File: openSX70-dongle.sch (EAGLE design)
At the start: 22 parts

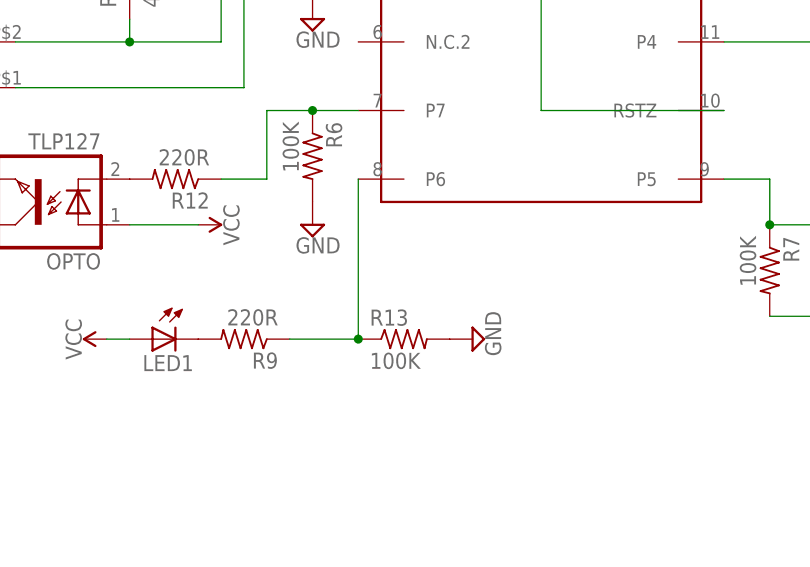
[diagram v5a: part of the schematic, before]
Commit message: P7 and P6 had a pulldown resistor when a pullup was needed. More D'ho! stuff.
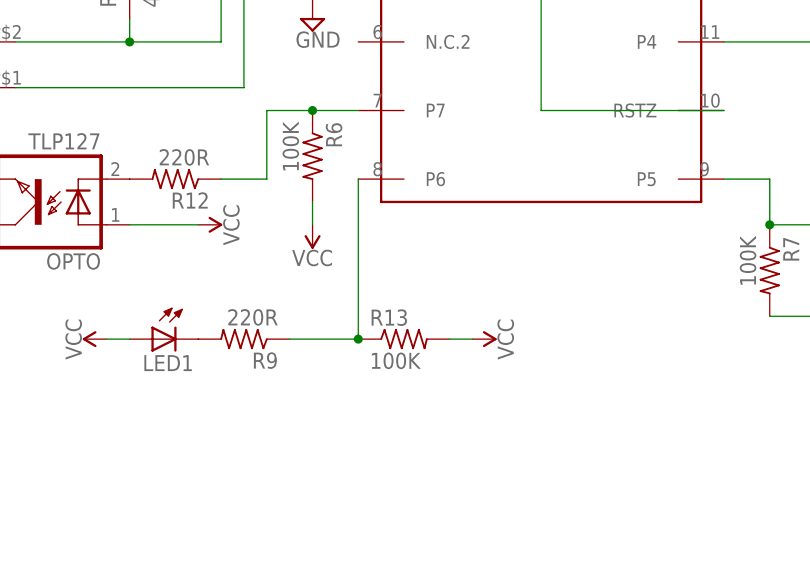
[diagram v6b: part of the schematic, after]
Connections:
- net GND: no longer R13.2, R6.2
- net VCC: now also R13.2, R6.2
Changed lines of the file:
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@@
 <part name="OPTO" library="openSX70" deviceset="TLP127" device="" value="TLP127"/>
 <part name="R12" library="rcl" library_urn="urn:adsk.eagle:library:334" deviceset="R-US_" device="M0805" package3d_urn="urn:adsk.eagle:package:23556/1" value="220R"/>
-<part name="GND-ISO10" library="supply2" library_urn="urn:adsk.eagle:library:372" deviceset="GND" device=""/>
 <part name="R13" library="rcl" library_urn="urn:adsk.eagle:library:334" deviceset="R-US_" device="M0805" package3d_urn="urn:adsk.eagle:package:23556/1" value="100K"/>
 <part name="SUPPLY8" library="SparkFun-PowerSymbols" library_urn="urn:adsk.eagle:library:530" deviceset="VCC" device=""/>
 <part name="PC-FLASH" library="SparkFun-Connectors" deviceset="AUDIO_JACK_3.5MM" device="_PTH"/>
 <part name="FRAME1" library="frames" library_urn="urn:adsk.eagle:library:229" deviceset="DINA4_L" device=""/>
-<part name="GND-ISO3" library="supply2" library_urn="urn:adsk.eagle:library:372" deviceset="GND" device=""/>
 <part name="TP+" library="wirepad" library_urn="urn:adsk.eagle:library:412" deviceset="SMD2" device="" package3d_urn="urn:adsk.eagle:package:30839/1"/>
 <part name="TP-" library="wirepad" library_urn="urn:adsk.eagle:library:412" deviceset="SMD2" device="" package3d_urn="urn:adsk.eagle:package:30839/1"/>
@@
 <part name="GND-ISO11" library="supply2" library_urn="urn:adsk.eagle:library:372" deviceset="GND" device=""/>
 <part name="GND-ISO12" library="supply2" library_urn="urn:adsk.eagle:library:372" deviceset="GND" device=""/>
+<part name="SUPPLY2" library="SparkFun-PowerSymbols" library_urn="urn:adsk.eagle:library:530" deviceset="VCC" device=""/>
+<part name="SUPPLY3" library="SparkFun-PowerSymbols" library_urn="urn:adsk.eagle:library:530" deviceset="VCC" device=""/>
 </parts>
 <sheets>
@@
 <instance part="OPTO" gate="G$1" x="78.74" y="50.8" rot="R180"/>
 <instance part="R12" gate="G$1" x="93.98" y="53.34" rot="R180"/>
-<instance part="GND-ISO10" gate="GND" x="109.22" y="48.26"/>
 <instance part="R13" gate="G$1" x="119.38" y="35.56"/>
 <instance part="SUPPLY8" gate="G$1" x="86.36" y="35.56" rot="R90"/>
@@
 <instance part="FRAME1" gate="G$1" x="-7.62" y="-15.24"/>
 <instance part="FRAME1" gate="G$2" x="154.94" y="-15.24"/>
-<instance part="GND-ISO3" gate="GND" x="127" y="35.56" rot="R90"/>
 <instance part="TP+" gate="1" x="99.06" y="99.06" rot="R270"/>
 <instance part="TP-" gate="1" x="76.2" y="127" rot="R270"/>
@@
 <instance part="GND-ISO11" gate="GND" x="96.52" y="116.84" rot="R270"/>
 <instance part="GND-ISO12" gate="GND" x="228.6" y="104.14" rot="R90"/>
+<instance part="SUPPLY2" gate="G$1" x="127" y="35.56" rot="R270"/>
+<instance part="SUPPLY3" gate="G$1" x="109.22" y="48.26" rot="R180"/>
 </instances>
 <busses>
@@
 <wire x1="86.36" y1="35.56" x2="88.9" y2="35.56" width="0.1524" layer="91"/>
 </segment>
+<segment>
+<pinref part="R6" gate="G$1" pin="2"/>
+<pinref part="SUPPLY3" gate="G$1" pin="VCC"/>
+<wire x1="109.22" y1="50.8" x2="109.22" y2="48.26" width="0.1524" layer="91"/>
+</segment>
+<segment>
+<pinref part="R13" gate="G$1" pin="2"/>
+<pinref part="SUPPLY2" gate="G$1" pin="VCC"/>
+<wire x1="124.46" y1="35.56" x2="127" y2="35.56" width="0.1524" layer="91"/>
+</segment>
 </net>
 <net name="N$1" class="0">
@@
 </segment>
 <segment>
-<pinref part="R6" gate="G$1" pin="2"/>
-<pinref part="GND-ISO10" gate="GND" pin="GND"/>
-</segment>
-<segment>
-<pinref part="R13" gate="G$1" pin="2"/>
-<pinref part="GND-ISO3" gate="GND" pin="GND"/>
-</segment>
-<segment>

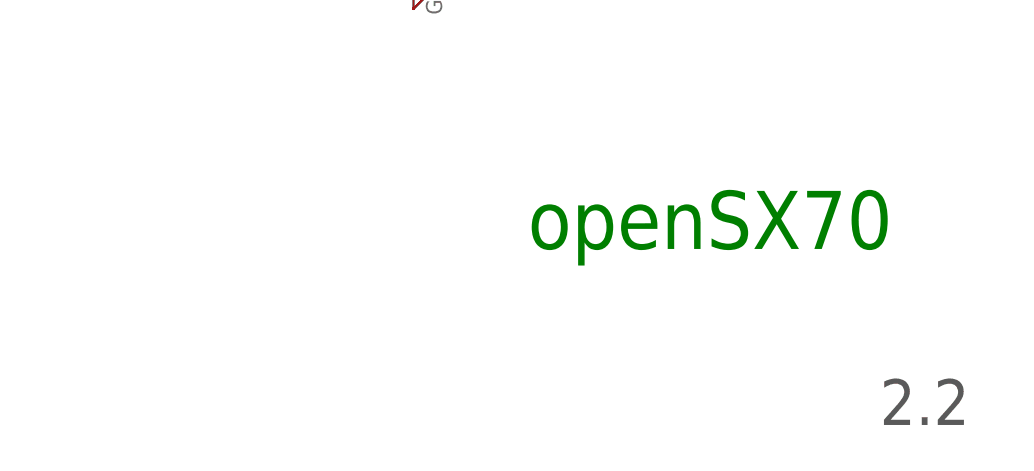
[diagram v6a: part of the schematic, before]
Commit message: Changed version number on schematic.
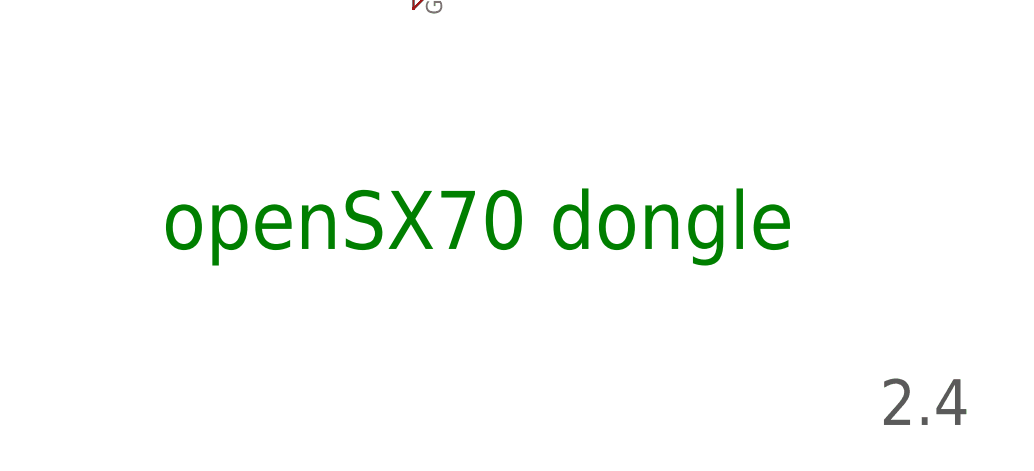
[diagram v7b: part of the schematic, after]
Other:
- note added: "2.4"
- note added: "openSX70 dongle"
- note removed: "2.2"
- note removed: "openSX70"
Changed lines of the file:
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@@
 <sheet>
 <plain>
-<text x="205.74" y="10.16" size="6.4516" layer="91">openSX70</text>
-<text x="244.856" y="-9.398" size="5.08" layer="97">2.2</text>
+<text x="165.1" y="10.16" size="6.4516" layer="91">openSX70 dongle</text>
+<text x="244.856" y="-9.398" size="5.08" layer="97">2.4</text>
 </plain>
 <instances>

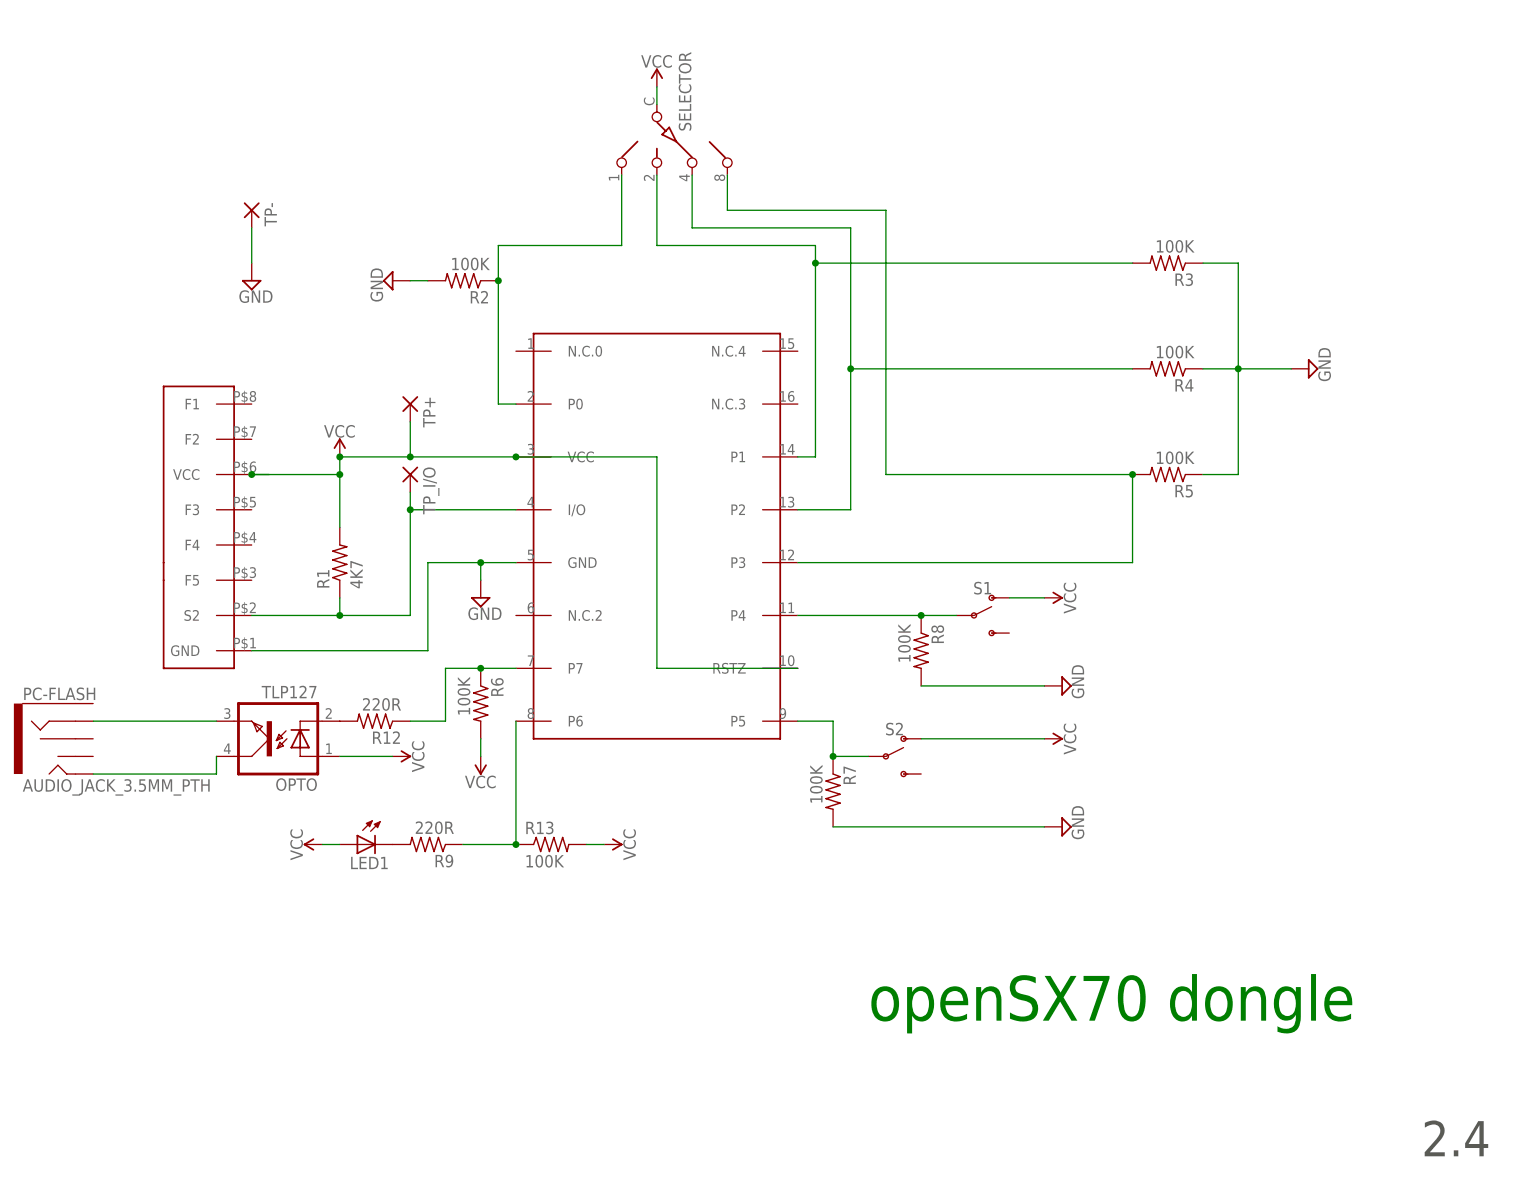
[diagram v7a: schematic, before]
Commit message: Had all the connections on the BCD wrong, now P0->pin2 DS->pin8 BCD P1->pin14 DS->pin4 BCD P2->pin13 DS->pin2 BCD P3->pin12 DS->pin1 BCD (same as in prototype). Also made the flash connector longer to allow for a case. Gone to version 2.6
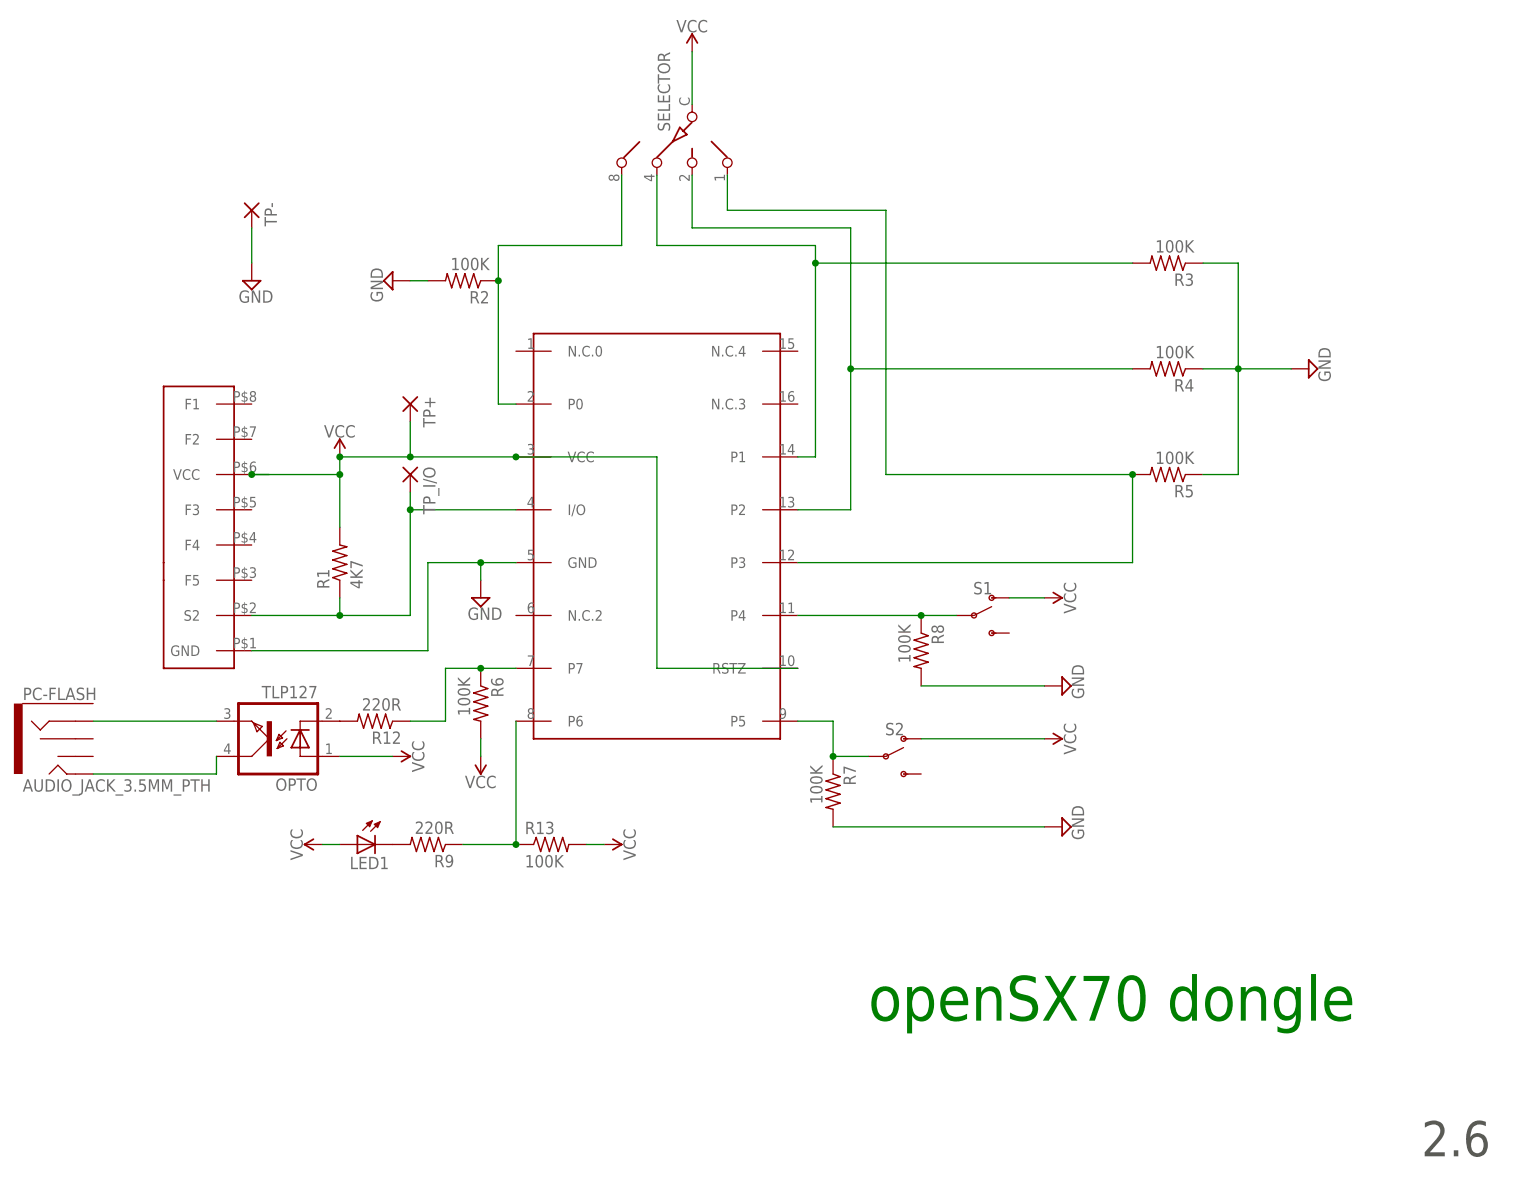
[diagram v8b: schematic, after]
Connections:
- net N$13: now also SELECTOR.1; no longer SELECTOR.8
- net N$3: now also SELECTOR.8; no longer SELECTOR.1
- net N$4: now also SELECTOR.4; no longer SELECTOR.2
- net N$5: now also SELECTOR.2; no longer SELECTOR.4
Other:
- note added: "2.6"
- note removed: "2.4"
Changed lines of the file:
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@@
 <?xml version="1.0" encoding="utf-8"?>
 <!DOCTYPE eagle SYSTEM "eagle.dtd">
-<eagle version="8.4.3">
+<eagle version="8.5.1">
 <drawing>
 <settings>
@@
 <plain>
 <text x="165.1" y="10.16" size="6.4516" layer="91">openSX70 dongle</text>
-<text x="244.856" y="-9.398" size="5.08" layer="97">2.4</text>
+<text x="244.856" y="-9.398" size="5.08" layer="97">2.6</text>
 </plain>
 <instances>
@@
 <instance part="R8" gate="G$1" x="172.72" y="63.5" rot="R270"/>
 <instance part="R9" gate="G$1" x="101.6" y="35.56" rot="R180"/>
-<instance part="SELECTOR" gate="G$1" x="134.62" y="137.16" rot="R270"/>
-<instance part="SUPPLY4" gate="G$1" x="134.62" y="144.78"/>
+<instance part="SELECTOR" gate="G$1" x="139.7" y="137.16" rot="MR270"/>
+<instance part="SUPPLY4" gate="G$1" x="139.7" y="149.86"/>
 <instance part="GND-ISO1" gate="GND" x="109.22" y="71.12"/>
 <instance part="S1" gate="1" x="180.34" y="68.58"/>
@@
 <net name="VCC" class="0">
 <segment>
-<pinref part="SUPPLY4" gate="G$1" pin="VCC"/>
-<pinref part="SELECTOR" gate="G$1" pin="C"/>
-<wire x1="134.62" y1="144.78" x2="134.62" y2="142.24" width="0.1524" layer="91"/>
-</segment>
-<segment>
 <pinref part="S1" gate="1" pin="O"/>
 <pinref part="SUPPLY5" gate="G$1" pin="VCC"/>
@@
 <wire x1="124.46" y1="35.56" x2="127" y2="35.56" width="0.1524" layer="91"/>
 </segment>
+<segment>
+<pinref part="SUPPLY4" gate="G$1" pin="VCC"/>
+<pinref part="SELECTOR" gate="G$1" pin="C"/>
+<wire x1="139.7" y1="149.86" x2="139.7" y2="142.24" width="0.1524" layer="91"/>
+</segment>
 </net>
 <net name="N$1" class="0">
@@
 <wire x1="111.76" y1="116.84" x2="111.76" y2="121.92" width="0.1524" layer="91"/>
 <wire x1="111.76" y1="121.92" x2="129.54" y2="121.92" width="0.1524" layer="91"/>
-<pinref part="SELECTOR" gate="G$1" pin="1"/>
-<wire x1="129.54" y1="121.92" x2="129.54" y2="132.08" width="0.1524" layer="91"/>
 <pinref part="R2" gate="G$1" pin="1"/>
 <junction x="111.76" y="116.84"/>
+<wire x1="129.54" y1="121.92" x2="129.54" y2="132.08" width="0.1524" layer="91"/>
+<pinref part="SELECTOR" gate="G$1" pin="8"/>
 </segment>
 </net>
 <net name="N$4" class="0">
 <segment>
-<pinref part="SELECTOR" gate="G$1" pin="2"/>
-<wire x1="134.62" y1="132.08" x2="134.62" y2="121.92" width="0.1524" layer="91"/>
 <wire x1="134.62" y1="121.92" x2="157.48" y2="121.92" width="0.1524" layer="91"/>
 <pinref part="DS2408" gate="G$1" pin="P1"/>
@@
 <wire x1="203.2" y1="119.38" x2="157.48" y2="119.38" width="0.1524" layer="91"/>
 <junction x="157.48" y="119.38"/>
+<pinref part="SELECTOR" gate="G$1" pin="4"/>
+<wire x1="134.62" y1="132.08" x2="134.62" y2="121.92" width="0.1524" layer="91"/>
 </segment>
 </net>
 <net name="N$5" class="0">
 <segment>
-<pinref part="SELECTOR" gate="G$1" pin="4"/>
-<wire x1="139.7" y1="132.08" x2="139.7" y2="124.46" width="0.1524" layer="91"/>
 <wire x1="139.7" y1="124.46" x2="162.56" y2="124.46" width="0.1524" layer="91"/>
 <pinref part="DS2408" gate="G$1" pin="P2"/>
@@
 <wire x1="203.2" y1="104.14" x2="162.56" y2="104.14" width="0.1524" layer="91"/>
 <junction x="162.56" y="104.14"/>
+<pinref part="SELECTOR" gate="G$1" pin="2"/>
+<wire x1="139.7" y1="132.08" x2="139.7" y2="124.46" width="0.1524" layer="91"/>
 </segment>
 </net>
@@
 <wire x1="203.2" y1="88.9" x2="167.64" y2="88.9" width="0.1524" layer="91"/>
 <junction x="203.2" y="88.9"/>
-<pinref part="SELECTOR" gate="G$1" pin="8"/>
 <wire x1="167.64" y1="127" x2="144.78" y2="127" width="0.1524" layer="91"/>
-<wire x1="144.78" y1="127" x2="144.78" y2="132.08" width="0.1524" layer="91"/>
 <wire x1="167.64" y1="88.9" x2="167.64" y2="127" width="0.1524" layer="91"/>
-</segment>
-</net>
+<pinref part="SELECTOR" gate="G$1" pin="1"/>
+<wire x1="144.78" y1="132.08" x2="144.78" y2="127" width="0.1524" layer="91"/>
+</segment>
+</net>
